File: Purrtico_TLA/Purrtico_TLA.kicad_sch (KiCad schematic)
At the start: 66 parts, among them J1 XLR3, J3 Conn_01x02, J4 XLR3, J5 Conn_01x02, J7 Conn_02x05_Odd_Even, U1 OPA1679, U2 OPA1679

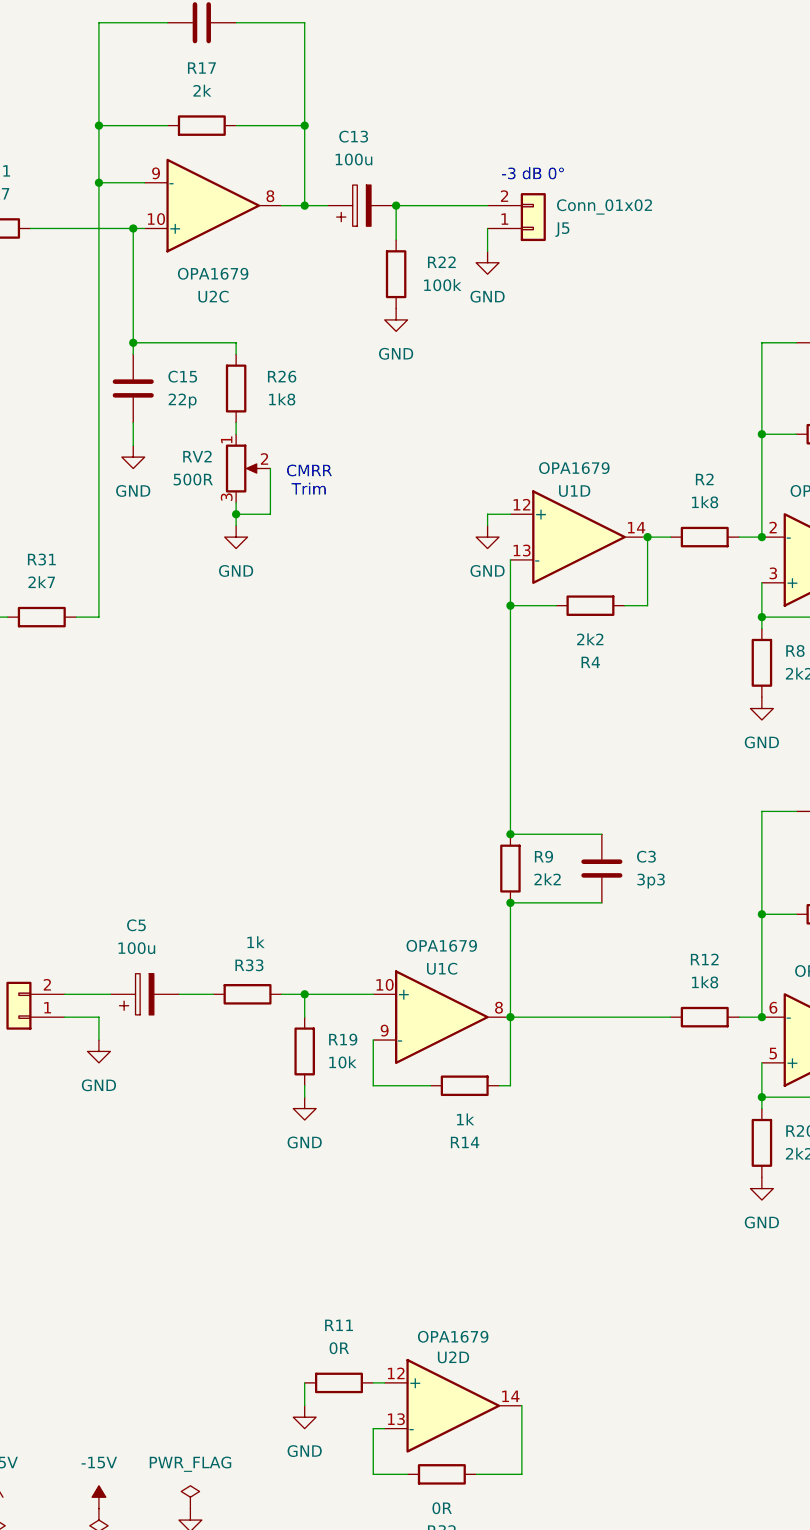
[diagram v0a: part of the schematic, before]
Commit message: update annotation
parity with final r00
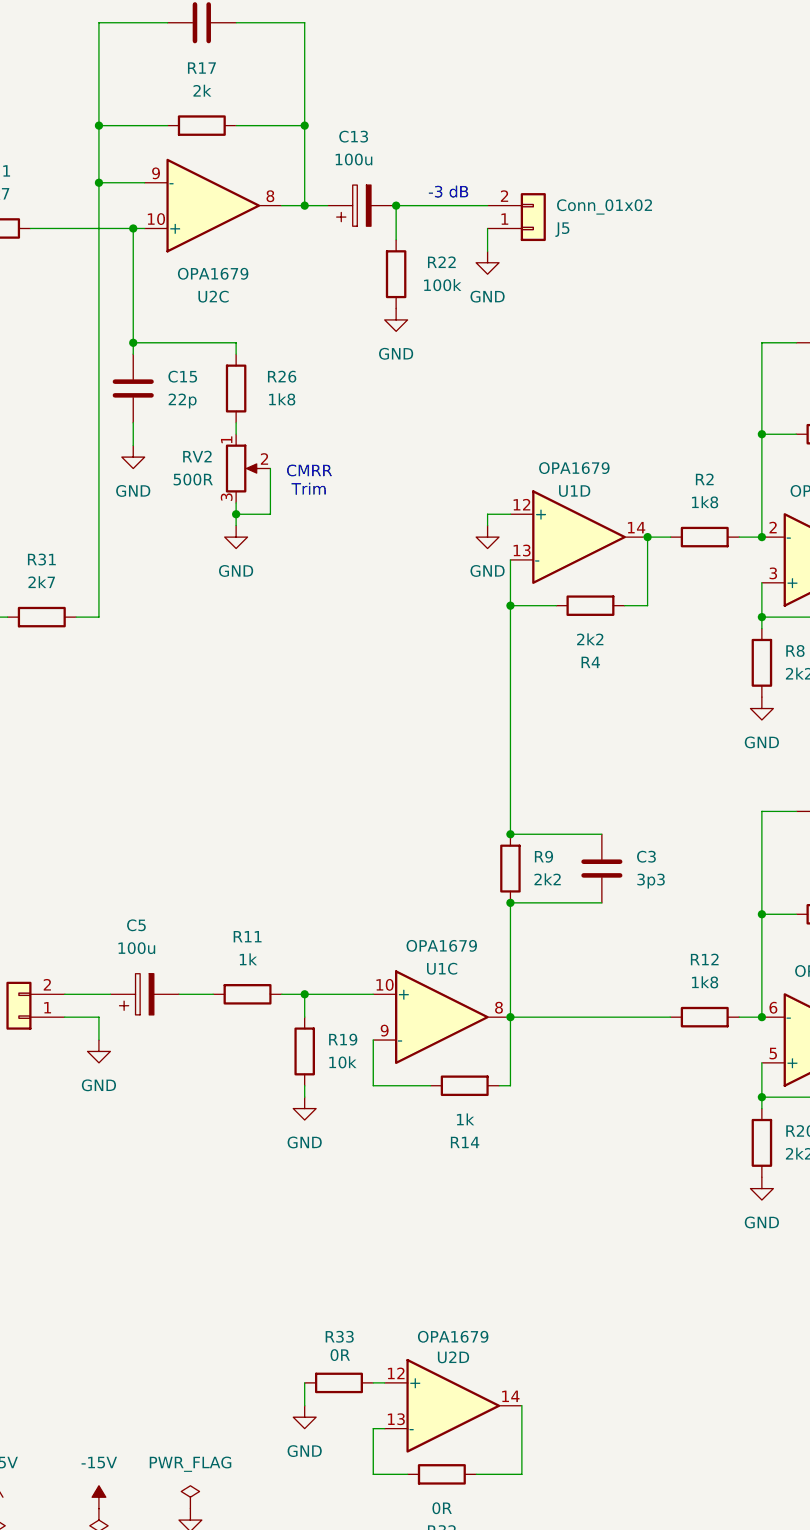
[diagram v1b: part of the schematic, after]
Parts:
- R11: value 0R -> 1k
- R33: value 1k -> 0R
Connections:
- net GND: now also R33.2; no longer R11.2
- net at R19.2, U1.10 (+): now also R11.1; no longer R33.1
- net at U2.12 (+): now also R33.1; no longer R11.1
- net at C5.2: now also R11.2; no longer R33.2
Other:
- note added: "-3 dB"
- note removed: "-3 dB 0°"
- moved on the sheet: R11, R33
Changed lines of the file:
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@@
 		)
 	)
-	(text "-3 dB 0°"
+	(text "-3 dB"
 		(exclude_from_sim no)
-		(at 172.72 41.91 0)
+		(at 163.322 43.942 0)
 		(effects
 			(font
@@
 	(symbol
 		(lib_id "Device:R")
-		(at 151.13 175.26 270)
+		(at 140.97 132.08 270)
 		(unit 1)
 		(exclude_from_sim no)
@@
 		(fields_autoplaced yes)
 		(property "Reference" "R11"
-			(at 151.13 168.91 90)
+			(at 140.97 125.73 90)
 			(effects
 				(font
@@
 			)
 		)
-		(property "Value" "0R"
-			(at 151.13 171.45 90)
+		(property "Value" "1k"
+			(at 140.97 128.27 90)
 			(effects
 				(font
@@
 		)
 		(property "Footprint" "Resistor_SMD:R_1206_3216Metric"
-			(at 151.13 173.482 90)
+			(at 140.97 130.302 90)
 			(effects
 				(font
@@
 		)
 		(property "Datasheet" "~"
-			(at 151.13 175.26 0)
+			(at 140.97 132.08 0)
 			(effects
 				(font
@@
 		)
 		(property "Description" ""
-			(at 151.13 175.26 0)
+			(at 140.97 132.08 0)
 			(effects
 				(font
@@
 	(symbol
 		(lib_id "Device:R")
-		(at 140.97 132.08 270)
+		(at 151.13 175.26 270)
 		(unit 1)
 		(exclude_from_sim no)
@@
 		(dnp no)
 		(property "Reference" "R33"
-			(at 142.875 128.905 90)
+			(at 152.908 170.18 90)
 			(effects
 				(font
@@
 			)
 		)
-		(property "Value" "1k"
-			(at 142.875 126.365 90)
+		(property "Value" "0R"
+			(at 152.4 172.212 90)
 			(effects
 				(font
@@
 		)
 		(property "Footprint" "Resistor_SMD:R_1206_3216Metric"
-			(at 140.97 130.302 90)
+			(at 151.13 173.482 90)
 			(effects
 				(font
@@
 		)
 		(property "Datasheet" "~"
-			(at 140.97 132.08 0)
+			(at 151.13 175.26 0)
 			(effects
 				(font
@@
 		)
 		(property "Description" ""
-			(at 140.97 132.08 0)
+			(at 151.13 175.26 0)
 			(effects
 				(font

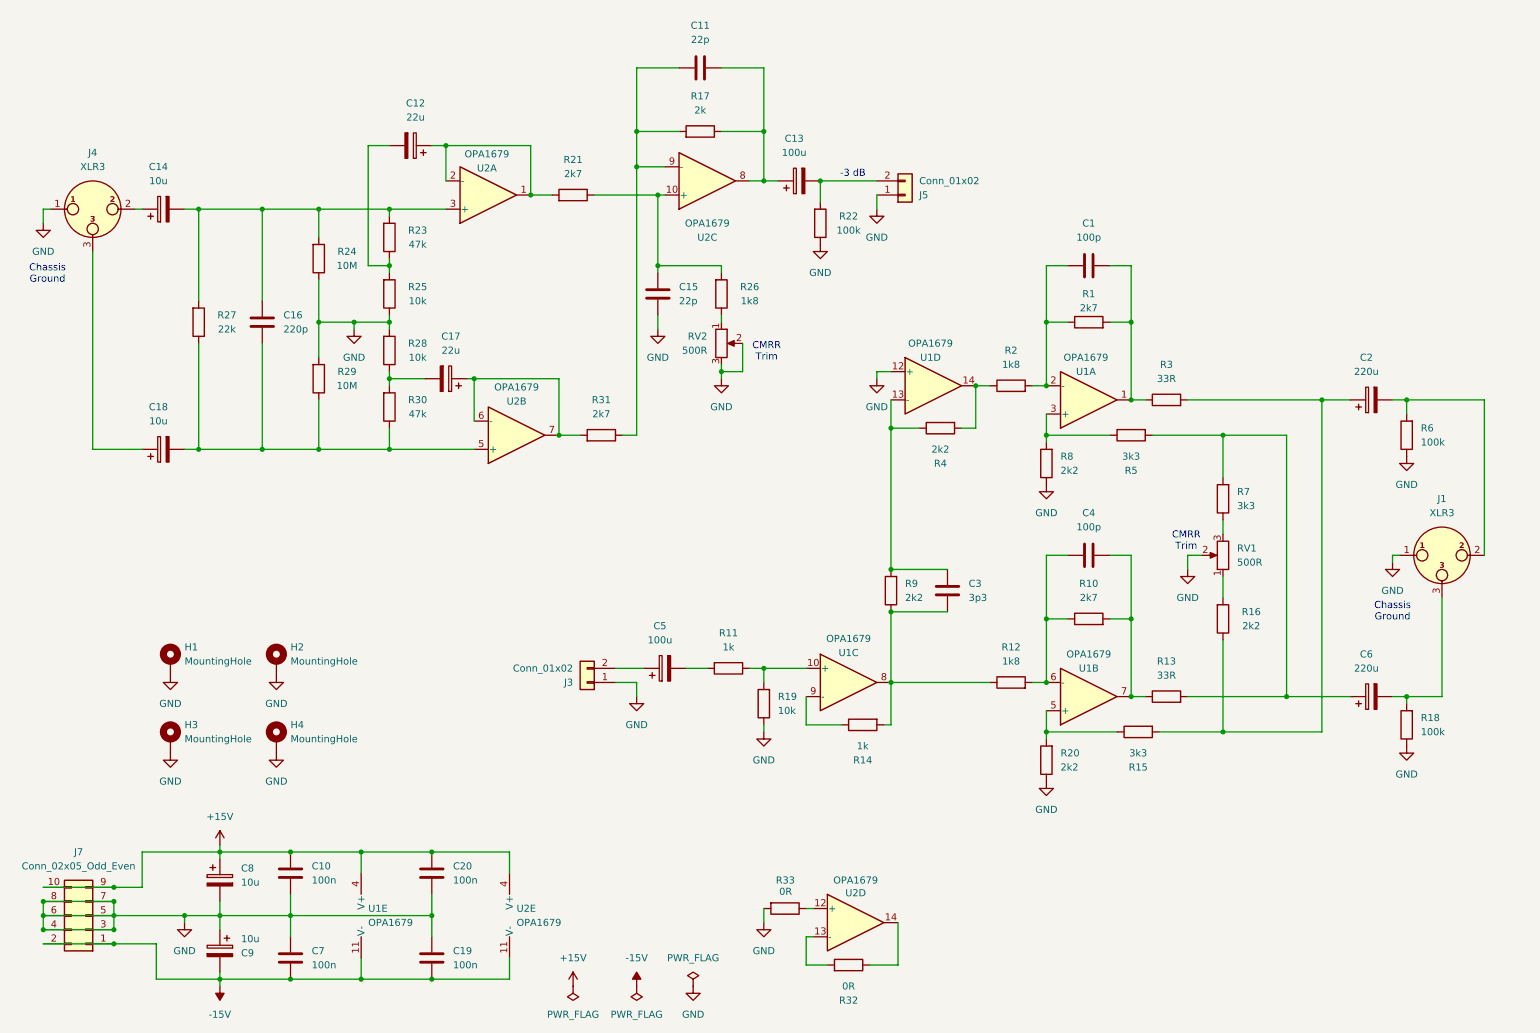
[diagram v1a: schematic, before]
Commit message: added optional HPF
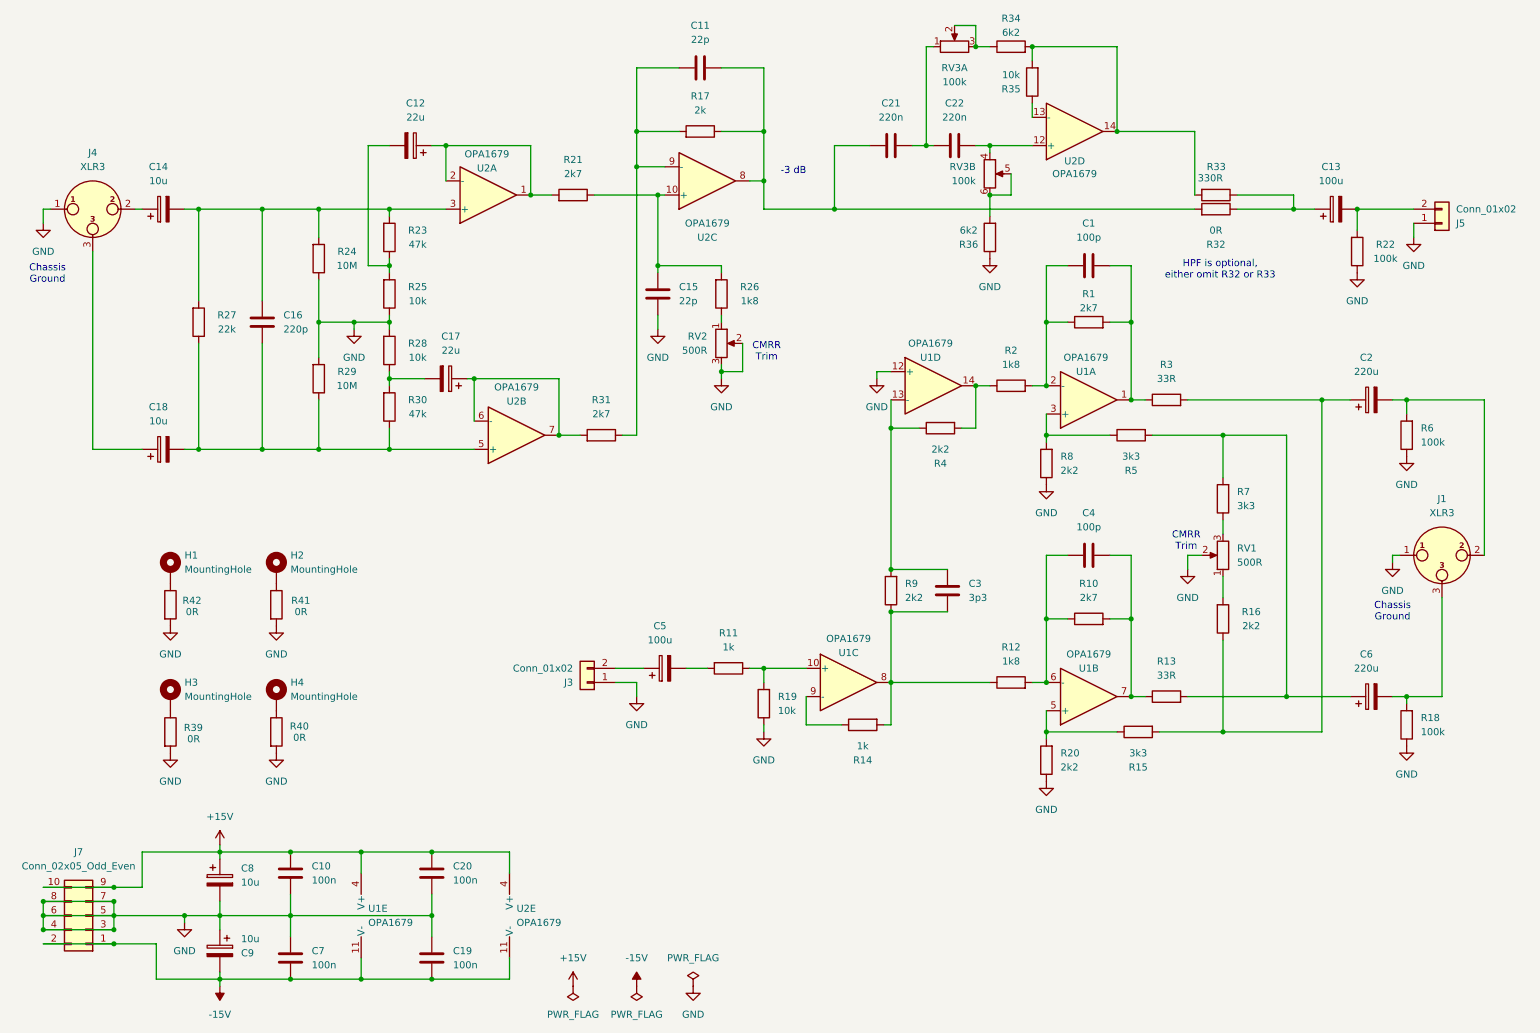
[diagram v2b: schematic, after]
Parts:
- added C21, C22: 220n, Capacitor_THT:C_Rect_L7.2mm_W2.5mm_P5.00mm_FKS2_FKP2_MKS2_MKP2, symbol Device:C
- added R34, R36: 6k2, Resistor_SMD:R_1206_3216Metric, symbol Device:R
- added R35: 10k, Resistor_SMD:R_1206_3216Metric, symbol Device:R
- added R39, R40, R41, R42: 0R, Resistor_SMD:R_1206_3216Metric, symbol Device:R
- added RV3: 100k, Connector_PinHeader_2.54mm:PinHeader_2x03_P2.54mm_Vertical, symbol Device:R_Potentiometer_Dual_Separate
- R33: value 0R -> 330R
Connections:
- net GND: now also R36.1, R39.2, R40.2, R41.2, R42.2; no longer H1.1, H2.1, H3.1, H4.1, R33.2
- net at C11.1, R17.1, U2.8: now also R32.2, C21.1; no longer C13.1
- net at R32.1: now also C13.1, R33.1; no longer U2.14
- net at U2.13 (-): now also R35.1; no longer R32.2
- net at U2.12 (+): now also C22.2, RV3.4; no longer R33.1
- new net: H3.1, R39.1
- new net: C21.2, C22.1, RV3.1
- new net: H4.1, R40.1
- new net: R34.1, RV3.2, RV3.3
- new net: R33.2, R34.2, R35.2, U2.14
- new net: H2.1, R41.1
- new net: H1.1, R42.1
- new net: R36.2, RV3.5, RV3.6
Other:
- note added: "HPF is optional, either omit R32 or R33"
- moved on the sheet: C13, H1, H2, H3, H4, J5, R22, R32, R33, U2D

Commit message: switch HPF knob
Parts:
- RV3: value 100k -> 100k log
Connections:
- net at C21.2, C22.1: now also RV3.2, RV3.3; no longer RV3.1
- net at C22.2, U2.12 (+): now also RV3.5, RV3.6; no longer RV3.4
- new net: R34.1, RV3.1
- new net: R36.2, RV3.4
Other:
- moved on the sheet: RV3A
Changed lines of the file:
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@@
 	)
 	(junction
-		(at 187.96 46.99)
-		(diameter 0)
-		(color 0 0 0 0)
-	)
-	(junction
 		(at 242.57 49.53)
 		(diameter 0)
@@
 	)
 	(junction
+		(at 176.53 20.32)
+		(diameter 0)
+		(color 0 0 0 0)
+	)
+	(junction
 		(at 57.15 49.53)
 		(diameter 0)
@@
 	)
 	(junction
-		(at 185.42 20.32)
-		(diameter 0)
-		(color 0 0 0 0)
-	)
-	(junction
 		(at 124.46 35.56)
 		(diameter 0)
@@
 	)
 	(junction
+		(at 191.77 38.1)
+		(diameter 0)
+		(color 0 0 0 0)
+	)
+	(junction
 		(at 49.53 165.1)
 		(diameter 0)
@@
 	(wire
 		(pts
-			(xy 185.42 16.51) (xy 185.42 20.32)
-		)
-		(stroke
-			(width 0)
-			(type default)
-		)
-	)
-	(wire
-		(pts
 			(xy 262.89 137.16) (xy 269.24 137.16)
 		)
@@
 	(wire
 		(pts
-			(xy 191.77 43.18) (xy 191.77 46.99)
-		)
-		(stroke
-			(width 0)
-			(type default)
-		)
-	)
-	(wire
-		(pts
 			(xy 224.79 46.99) (xy 224.79 35.56)
 		)
@@
 	(wire
 		(pts
-			(xy 181.61 16.51) (xy 185.42 16.51)
+			(xy 62.23 187.96) (xy 74.93 187.96)
 		)
 		(stroke
@@
 	(wire
 		(pts
-			(xy 62.23 187.96) (xy 74.93 187.96)
+			(xy 90.17 38.1) (xy 105.41 38.1)
 		)
 		(stroke
@@
 	(wire
 		(pts
-			(xy 90.17 38.1) (xy 105.41 38.1)
+			(xy 213.36 123.19) (xy 209.55 123.19)
 		)
 		(stroke
@@
 	(wire
 		(pts
-			(xy 213.36 123.19) (xy 209.55 123.19)
+			(xy 242.57 46.99) (xy 232.41 46.99)
 		)
 		(stroke
@@
 	(wire
 		(pts
-			(xy 242.57 46.99) (xy 232.41 46.99)
+			(xy 198.12 59.69) (xy 201.93 59.69)
 		)
 		(stroke
@@
 	(wire
 		(pts
-			(xy 198.12 59.69) (xy 201.93 59.69)
+			(xy 176.53 38.1) (xy 177.8 38.1)
 		)
 		(stroke
@@
 	(wire
 		(pts
-			(xy 176.53 38.1) (xy 177.8 38.1)
+			(xy 187.96 38.1) (xy 191.77 38.1)
 		)
 		(stroke
@@
 	(wire
 		(pts
-			(xy 187.96 38.1) (xy 195.58 38.1)
+			(xy 101.6 168.91) (xy 101.6 165.1)
 		)
 		(stroke
@@
 	(wire
 		(pts
-			(xy 101.6 168.91) (xy 101.6 165.1)
+			(xy 191.77 38.1) (xy 191.77 43.18)
 		)
 		(stroke
@@
 	(wire
 		(pts
+			(xy 181.61 16.51) (xy 176.53 16.51)
+		)
+		(stroke
+			(width 0)
+			(type default)
+		)
+	)
+	(wire
+		(pts
 			(xy 45.72 92.71) (xy 45.72 73.66)
 		)
@@
 	(wire
 		(pts
+			(xy 191.77 38.1) (xy 195.58 38.1)
+		)
+		(stroke
+			(width 0)
+			(type default)
+		)
+	)
+	(wire
+		(pts
 			(xy 229.87 143.51) (xy 247.65 143.51)
 		)
@@
 	(wire
 		(pts
+			(xy 176.53 16.51) (xy 176.53 20.32)
+		)
+		(stroke
+			(width 0)
+			(type default)
+		)
+	)
+	(wire
+		(pts
 			(xy 247.65 83.82) (xy 247.65 143.51)
 		)
@@
 	(wire
 		(pts
-			(xy 191.77 46.99) (xy 187.96 46.99)
-		)
-		(stroke
-			(width 0)
-			(type default)
-		)
-	)
-	(wire
-		(pts
 			(xy 124.46 134.62) (xy 124.46 137.16)
 		)
@@
 	(text "HPF is optional,\neither omit R32 or R33 "
 		(exclude_from_sim no)
-		(at 229.362 60.452 0)
+		(at 238.76 38.354 0)
 		(effects
 			(font
@@
 	(symbol
 		(lib_id "Device:R_Potentiometer_Dual_Separate")
-		(at 181.61 20.32 90)
+		(at 181.61 20.32 270)
+		(mirror x)
 		(unit 1)
 		(exclude_from_sim no)
@@
 		(on_board yes)
 		(dnp no)
-		(fields_autoplaced yes)
 		(property "Reference" "RV3"
 			(at 181.61 24.13 90)
@@
 			)
 		)
-		(property "Value" "100k"
+		(property "Value" "100k log"
 			(at 181.61 26.67 90)
 			(effects
@@
 		(lib_id "Device:R_Potentiometer_Dual_Separate")
 		(at 187.96 43.18 0)
+		(mirror x)
 		(unit 2)
 		(exclude_from_sim no)
@@
 		(on_board yes)
 		(dnp no)
-		(fields_autoplaced yes)
 		(property "Reference" "RV3"
-			(at 185.42 41.9099 0)
+			(at 185.42 44.4501 0)
 			(effects
 				(font
@@
 			)
 		)
-		(property "Value" "100k"
-			(at 185.42 44.4499 0)
+		(property "Value" "100k log"
+			(at 185.42 41.9101 0)
 			(effects
 				(font

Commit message: added fabrication outputs
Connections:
- net at C21.2, C22.1: now also RV3.1; no longer RV3.2, RV3.3
- net at R34.1: now also RV3.2, RV3.3; no longer RV3.1
- net at RV3.4: now also C22.2, U2.12 (+); no longer R36.2
- net at RV3.5, RV3.6: now also R36.2; no longer C22.2, U2.12 (+)
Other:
- moved on the sheet: RV3A
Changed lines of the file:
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@@
 	(title_block
 		(title "Purrtico TLA")
-		(date "2024-08-15")
+		(date "2024-08-16")
 		(rev "01")
 		(company "Greybox Audio")
@@
 	)
 	(junction
-		(at 176.53 20.32)
+		(at 57.15 49.53)
 		(diameter 0)
 		(color 0 0 0 0)
 	)
 	(junction
-		(at 57.15 49.53)
+		(at 170.18 114.3)
 		(diameter 0)
 		(color 0 0 0 0)
 	)
 	(junction
-		(at 170.18 114.3)
+		(at 187.96 48.26)
 		(diameter 0)
 		(color 0 0 0 0)
@@
 	)
 	(junction
+		(at 186.69 20.32)
+		(diameter 0)
+		(color 0 0 0 0)
+	)
+	(junction
 		(at 170.18 134.62)
 		(diameter 0)
@@
 	)
 	(junction
-		(at 191.77 38.1)
-		(diameter 0)
-		(color 0 0 0 0)
-	)
-	(junction
 		(at 49.53 165.1)
 		(diameter 0)
@@
 	(wire
 		(pts
+			(xy 186.69 16.51) (xy 186.69 20.32)
+		)
+		(stroke
+			(width 0)
+			(type default)
+		)
+	)
+	(wire
+		(pts
 			(xy 62.23 176.53) (xy 87.63 176.53)
 		)
@@
 	(wire
 		(pts
+			(xy 181.61 16.51) (xy 186.69 16.51)
+		)
+		(stroke
+			(width 0)
+			(type default)
+		)
+	)
+	(wire
+		(pts
 			(xy 210.82 35.56) (xy 210.82 20.32)
 		)
@@
 	(wire
 		(pts
+			(xy 186.69 20.32) (xy 187.96 20.32)
+		)
+		(stroke
+			(width 0)
+			(type default)
+		)
+	)
+	(wire
+		(pts
 			(xy 80.01 80.01) (xy 86.36 80.01)
 		)
@@
 	(wire
 		(pts
-			(xy 185.42 20.32) (xy 187.96 20.32)
+			(xy 185.42 20.32) (xy 186.69 20.32)
 		)
 		(stroke
@@
 	(wire
 		(pts
+			(xy 191.77 43.18) (xy 191.77 48.26)
+		)
+		(stroke
+			(width 0)
+			(type default)
+		)
+	)
+	(wire
+		(pts
 			(xy 217.17 90.17) (xy 229.87 90.17)
 		)
@@
 	(wire
 		(pts
-			(xy 187.96 38.1) (xy 191.77 38.1)
+			(xy 187.96 38.1) (xy 195.58 38.1)
 		)
 		(stroke
@@
 	(wire
 		(pts
-			(xy 191.77 38.1) (xy 191.77 43.18)
-		)
-		(stroke
-			(width 0)
-			(type default)
-		)
-	)
-	(wire
-		(pts
 			(xy 87.63 38.1) (xy 90.17 38.1)
 		)
@@
 	(wire
 		(pts
-			(xy 181.61 16.51) (xy 176.53 16.51)
-		)
-		(stroke
-			(width 0)
-			(type default)
-		)
-	)
-	(wire
-		(pts
 			(xy 45.72 92.71) (xy 45.72 73.66)
 		)
@@
 	(wire
 		(pts
-			(xy 187.96 46.99) (xy 187.96 50.8)
+			(xy 187.96 46.99) (xy 187.96 48.26)
 		)
 		(stroke
@@
 	(wire
 		(pts
-			(xy 191.77 38.1) (xy 195.58 38.1)
-		)
-		(stroke
-			(width 0)
-			(type default)
-		)
-	)
-	(wire
-		(pts
 			(xy 229.87 143.51) (xy 247.65 143.51)
 		)
@@
 	(wire
 		(pts
+			(xy 187.96 48.26) (xy 187.96 50.8)
+		)
+		(stroke
+			(width 0)
+			(type default)
+		)
+	)
+	(wire
+		(pts
 			(xy 30.48 173.99) (xy 30.48 176.53)
 		)
@@
 	(wire
 		(pts
-			(xy 176.53 16.51) (xy 176.53 20.32)
-		)
-		(stroke
-			(width 0)
-			(type default)
-		)
-	)
-	(wire
-		(pts
 			(xy 247.65 83.82) (xy 247.65 143.51)
 		)
@@
 	(wire
 		(pts
+			(xy 191.77 48.26) (xy 187.96 48.26)
+		)
+		(stroke
+			(width 0)
+			(type default)
+		)
+	)
+	(wire
+		(pts
 			(xy 80.01 49.53) (xy 67.31 49.53)
 		)
@@
 	(symbol
 		(lib_id "Device:R_Potentiometer_Dual_Separate")
-		(at 181.61 20.32 270)
-		(mirror x)
+		(at 181.61 20.32 90)
 		(unit 1)
 		(exclude_from_sim no)
@@
 		(lib_id "Device:R_Potentiometer_Dual_Separate")
 		(at 187.96 43.18 0)
-		(mirror x)
 		(unit 2)
 		(exclude_from_sim no)
@@
 		(dnp no)
 		(property "Reference" "RV3"
-			(at 185.42 44.4501 0)
+			(at 185.42 41.9099 0)
 			(effects
 				(font
@@
 		)
 		(property "Value" "100k log"
-			(at 185.42 41.9101 0)
+			(at 185.42 44.4499 0)
 			(effects
 				(font
